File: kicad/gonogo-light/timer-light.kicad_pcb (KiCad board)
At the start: 2 copper layers, 108 x 97.3 mm, 62 parts, among them J1 Screw_Terminal_01x02, J2 Screw_Terminal_01x04, K1 FINDER-30.22, Q1 2N2222, Q2 2N2222, SW1 SW_DIP_x04, SW2 SW_DIP_x08, SW3 SW_DIP_x04, SW4 SW_DIP_x08, U1 4011, U10 4011, U11 4040, U12 4012, U13 4068, U2 4040, U3 4060, U4 4012, U5 4013, U6 4011, U7 4040, U8 4068, U9 4012, Y1 32,768 kHz

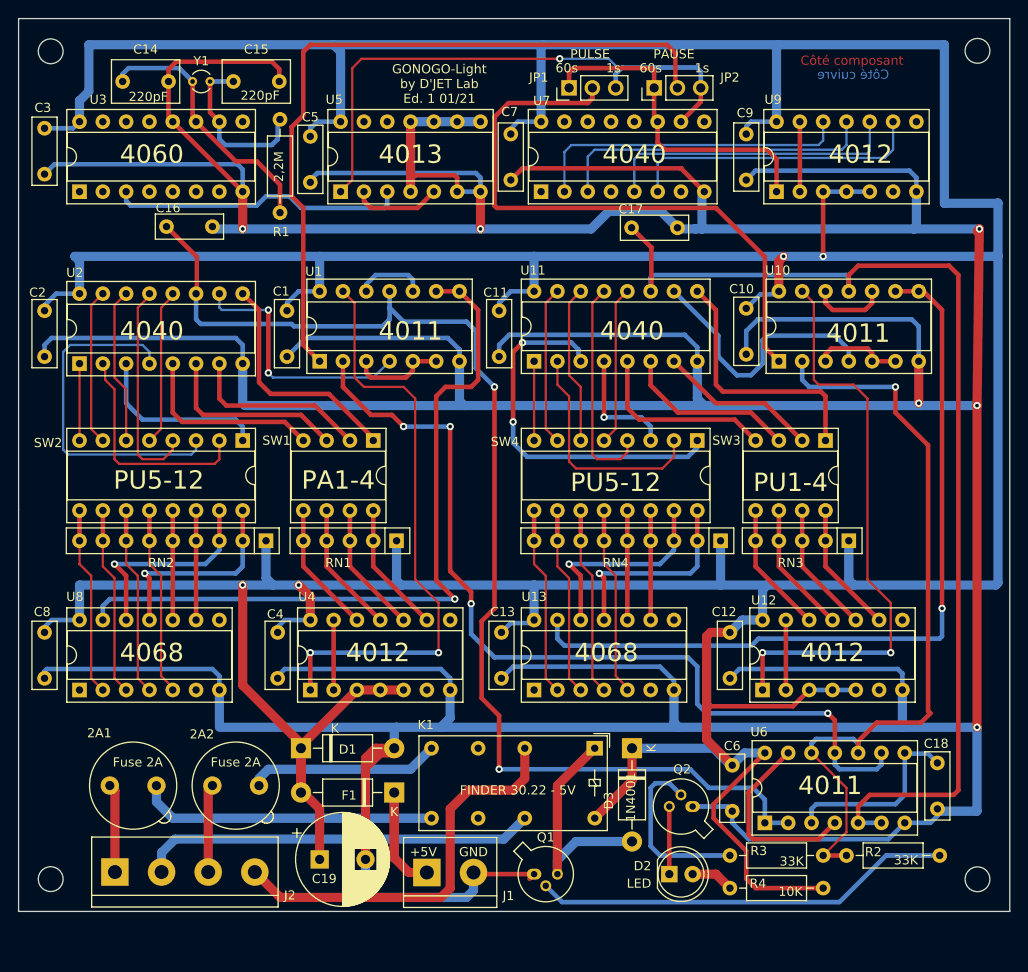
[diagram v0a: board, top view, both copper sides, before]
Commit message: correction des erreurs et ajout de capas de reset sur poweron
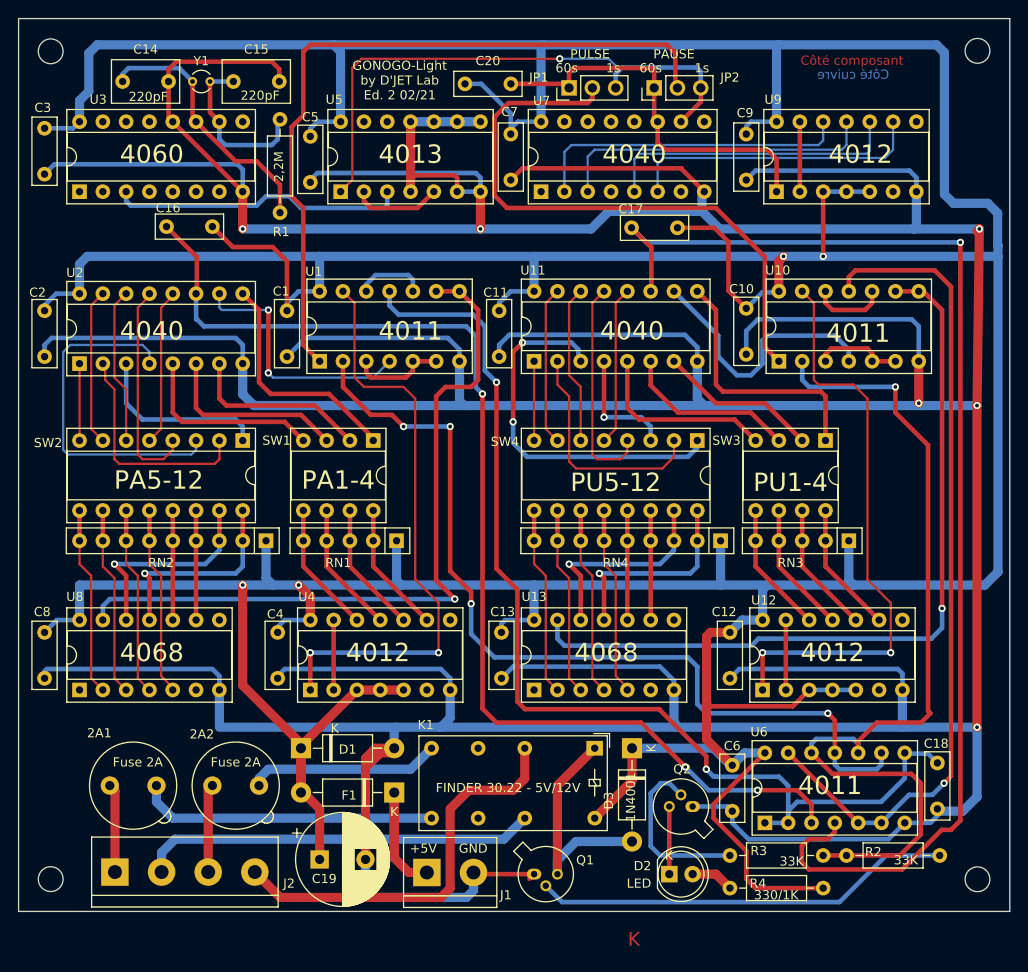
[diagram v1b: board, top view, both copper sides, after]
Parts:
- added C20: 100nF, Capacitor_THT:C_Rect_L7.2mm_W2.5mm_P5.00mm_FKS2_FKP2_MKS2_MKP2, F.Cu at (144.6, 48.0)
- R4: value 10k -> Voir Note 1
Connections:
- C16 pad 1: GND -> VDD
- C17 pad 1: GND -> VDD
- U1 pad 11: /RSTPA -> /&PA1-12
- U10 pad 11: /RSTPU -> /&PUA1-12
- U6 pad 1: /RSTPA -> /&PA1-12
- U6 pad 2: /RSTPA -> /&PA1-12
- U6 pad 3: /&PA1-12 -> /RSTPA
- U6 pad 4: /&PUA1-12 -> /RSTPU
- U6 pad 5: /RSTPU -> /&PUA1-12
- U6 pad 6: /RSTPU -> /&PUA1-12
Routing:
- net /&PA1-12: track 20.9 -> 118.6 mm, vias 0 -> 2
- net /&PUA1-12: track 21.0 -> 90.1 mm, vias 0 -> 1
- net VDD: track 649.9 -> 683.3 mm
- net /RSTPU: track 119.4 -> 134.1 mm, vias 0 -> 1
- net /PULSE_ENABLE: track 83.9 -> 98.0 mm
- net GND: track 775.1 -> 768.0 mm
- net /60sec: track 36.5 -> 43.0 mm
- net /RSTPA: track 132.1 -> 125.8 mm, vias 2 -> 3
- net /CLK-PULSE: track 66.1 -> 65.4 mm
- net Net-(U10-Pad8): track 86.2 -> 85.6 mm
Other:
- board text added: "330/1K"
- board text added: "FINDER 30.22 - 5V/12V"
- board text added: "GONOGO-Light by D'JET Lab Ed. 2 02/21"
- board text added: "K"
- board text added: "PA5-12"
- board text removed: "10K"
- board text removed: "FINDER 30.22 - 5V"
- board text removed: "GONOGO-Light by D'JET Lab Ed. 1 01/21"
